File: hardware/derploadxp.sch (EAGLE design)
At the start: 53 parts, among them IC3 TC7660SO-08, J1 AVR_SPI_PRG_6NS, J2 POWER_JACKPTH, U1 ATMEGA328P_PDIP

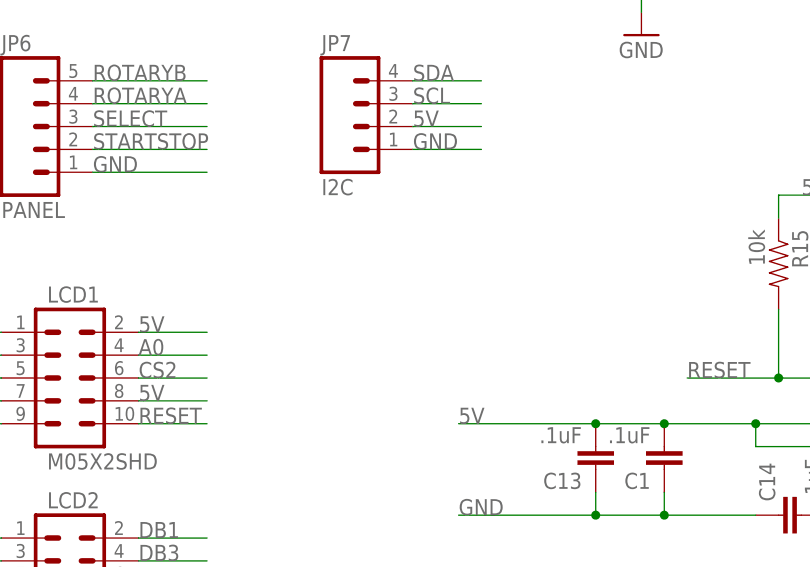
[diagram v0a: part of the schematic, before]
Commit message: Added 12V aux port
Addresses issue #11
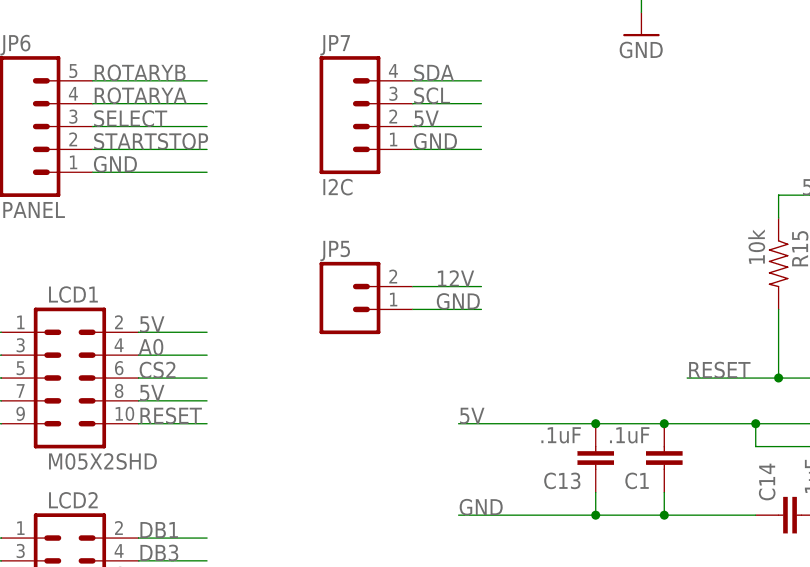
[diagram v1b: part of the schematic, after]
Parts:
- added JP5: (no value), SparkFun-Connectors:M02LOCK
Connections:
- net 12V: now also JP5.2
- net GND: now also JP5.1
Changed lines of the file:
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@@
 <?xml version="1.0" encoding="utf-8"?>
 <!DOCTYPE eagle SYSTEM "eagle.dtd">
-<eagle version="6.4">
+<eagle version="6.3">
 <drawing>
 <settings>
@@
 <part name="C15" library="SparkFun-Passives" deviceset="CAP" device="0805" value="22pf"/>
 <part name="R21" library="SparkFun-Electromechanical" deviceset="TRIMPOT" device="SMD"/>
+<part name="JP5" library="SparkFun-Connectors" deviceset="M02" device="LOCK"/>
 </parts>
 <sheets>
@@
 <instance part="C15" gate="G$1" x="-91.44" y="226.06" rot="R270"/>
 <instance part="R21" gate="R?" x="12.7" y="279.4" rot="R270"/>
+<instance part="JP5" gate="G$1" x="-119.38" y="266.7"/>
 </instances>
 <busses>
@@
 <label x="-111.76" y="284.48" size="1.778" layer="95"/>
 </segment>
+<segment>
+<pinref part="JP5" gate="G$1" pin="1"/>
+<wire x1="-111.76" y1="266.7" x2="-104.14" y2="266.7" width="0.1524" layer="91"/>
+<label x="-109.22" y="266.7" size="1.778" layer="95"/>
+</segment>
 </net>
 <net name="VSENSE" class="0">
@@
 <junction x="93.98" y="314.96"/>
 </segment>
-</net>
+<segment>
+<pinref part="JP5" gate="G$1" pin="2"/>
+<wire x1="-111.76" y1="269.24" x2="-104.14" y2="269.24" width="0.1524" layer="91"/>
+<label x="-109.22" y="269.24" size="1.778" layer="95"/>
+</segment>
+</net>

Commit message: added missing junctions and corrected other necessary errors, remainder were approved resolving Issue #10
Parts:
- J1: value AVR_SPI_PRG_6NS -> SPI
- renumbered U$3 to D1
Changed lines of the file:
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@@
 <?xml version="1.0" encoding="utf-8"?>
 <!DOCTYPE eagle SYSTEM "eagle.dtd">
-<eagle version="6.3">
+<eagle version="6.4">
 <drawing>
 <settings>
@@
 <parts>
 <part name="U1" library="SparkFun-DigitalIC" deviceset="ATMEGA328P_PDIP" device=""/>
-<part name="J1" library="SparkFun-Connectors" deviceset="AVR_SPI_PRG_6" device="NS"/>
+<part name="J1" library="SparkFun-Connectors" deviceset="AVR_SPI_PRG_6" device="NS" value="SPI"/>
 <part name="JP2" library="SparkFun-Connectors" deviceset="M03" device="LOCK"/>
 <part name="JP3" library="SparkFun-Connectors" deviceset="M03" device="LOCK"/>
@@
 <part name="C6" library="SparkFun-Passives" deviceset="CAP" device="0805" value=".1uf"/>
 <part name="JP1" library="SparkFun-Connectors" deviceset="M04" device="LOCK"/>
-<part name="U$3" library="SparkFun-DiscreteSemi" deviceset="DIODE-ZENER" device="-BZT52"/>
+<part name="D1" library="SparkFun-DiscreteSemi" deviceset="DIODE-ZENER" device="-BZT52"/>
 <part name="IC3" library="microchip_tc7660" deviceset="TC7660" device="SO-08"/>
 <part name="C7" library="SparkFun-Capacitors" deviceset="CAP_POL" device="C" value="10uF"/>
@@
 <instance part="C6" gate="G$1" x="193.04" y="289.56" rot="R180"/>
 <instance part="JP1" gate="G$1" x="233.68" y="302.26" rot="R180"/>
-<instance part="U$3" gate="G$1" x="182.88" y="287.02" rot="R90"/>
+<instance part="D1" gate="G$1" x="182.88" y="287.02" rot="R90"/>
 <instance part="IC3" gate="G$1" x="-30.48" y="297.18"/>
 <instance part="C7" gate="G$1" x="-172.72" y="309.88"/>
@@
 <pinref part="GND1" gate="1" pin="GND"/>
 <wire x1="-86.36" y1="299.72" x2="-86.36" y2="302.26" width="0.1524" layer="91"/>
+<junction x="-86.36" y="302.26"/>
 </segment>
 <segment>
@@
 <pinref part="GND4" gate="1" pin="GND"/>
 <wire x1="200.66" y1="281.94" x2="200.66" y2="279.4" width="0.1524" layer="91"/>
-<pinref part="U$3" gate="G$1" pin="A"/>
+<pinref part="D1" gate="G$1" pin="A"/>
 <wire x1="182.88" y1="284.48" x2="182.88" y2="281.94" width="0.1524" layer="91"/>
 <wire x1="182.88" y1="281.94" x2="193.04" y2="281.94" width="0.1524" layer="91"/>
@@
 <wire x1="-99.06" y1="226.06" x2="-99.06" y2="205.74" width="0.1524" layer="91"/>
 <wire x1="-99.06" y1="205.74" x2="-68.58" y2="205.74" width="0.1524" layer="91"/>
+<junction x="-99.06" y="226.06"/>
+<junction x="-68.58" y="205.74"/>
+<junction x="-68.58" y="203.2"/>
 </segment>
 <segment>
@@
 <wire x1="193.04" y1="294.64" x2="182.88" y2="294.64" width="0.1524" layer="91"/>
 <label x="170.18" y="294.64" size="1.778" layer="95"/>
-<pinref part="U$3" gate="G$1" pin="C"/>
+<pinref part="D1" gate="G$1" pin="C"/>
 <wire x1="182.88" y1="294.64" x2="170.18" y2="294.64" width="0.1524" layer="91"/>
 <wire x1="182.88" y1="289.56" x2="182.88" y2="294.64" width="0.1524" layer="91"/>
@@
 <wire x1="-190.5" y1="215.9" x2="-198.12" y2="215.9" width="0.1524" layer="91"/>
 <label x="-198.12" y="215.9" size="1.778" layer="95"/>
+<junction x="-190.5" y="215.9"/>
 </segment>
 <segment>
@@
 <wire x1="-205.74" y1="215.9" x2="-215.9" y2="215.9" width="0.1524" layer="91"/>
 <label x="-215.9" y="215.9" size="1.778" layer="95"/>
+<junction x="-205.74" y="215.9"/>
 </segment>
 <segment>
@@
 <pinref part="C12" gate="G$1" pin="1"/>
 <wire x1="-86.36" y1="233.68" x2="-81.28" y2="233.68" width="0.1524" layer="91"/>
+<junction x="-81.28" y="233.68"/>
 </segment>
 </net>
@@
 <wire x1="-86.36" y1="226.06" x2="-81.28" y2="226.06" width="0.1524" layer="91"/>
 <wire x1="-81.28" y1="226.06" x2="-81.28" y2="228.6" width="0.1524" layer="91"/>
+<junction x="-81.28" y="228.6"/>
 </segment>
 </net>
@@
 </sheet>
 </sheets>
+<errors>
+</errors>
 </schematic>
 </drawing>
